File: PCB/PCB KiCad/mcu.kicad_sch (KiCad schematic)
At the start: 12 parts, among them J1 ADC Debug, J2 LED Debug, J3 Qwiic, SW1 MCU_RESET, SW2 TRIGGER

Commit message: PCB at time of order
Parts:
- R17: value 82 -> 150
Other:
- note added: "potential problem logic is at 5v potential solution logic level shifter"
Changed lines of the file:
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@@
     (effects (font (size 3 3)) (justify left bottom))
+  )
+  (text "potential problem\nlogic is at 5v\npotential solution\nlogic level shifter\n\n"
+    (at 129.54 100.33 0)
+    (effects (font (size 1.27 1.27)) (justify left bottom))
   )
   (text "Connectors" (at 39.37 148.59 0)
@@
       (effects (font (size 1.27 1.27)) (justify right))
     )
-    (property "Value" "82" (id 1) (at 213.36 48.8949 0)
-      (effects (font (size 1.27 1.27)) (justify right))
-    )
+    (property "Value" "150" (id 1) (at 213.36 48.8949 0)
+      (effects (font (size 1.27 1.27)) (justify right))
+    )

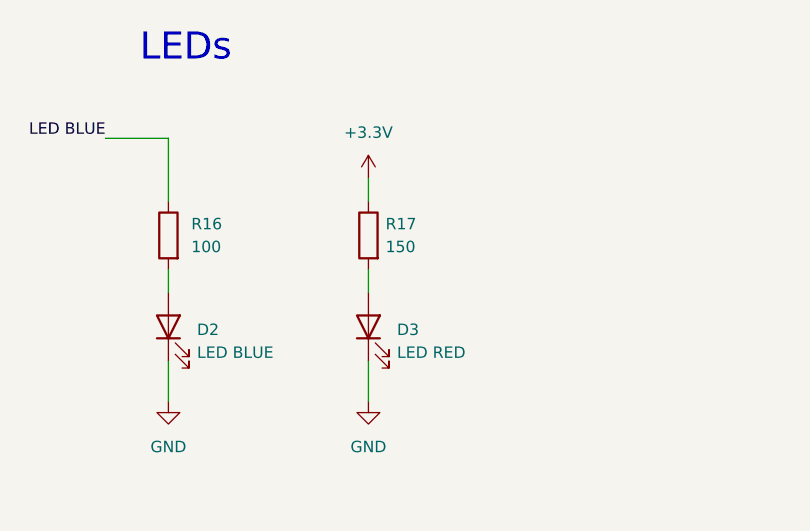
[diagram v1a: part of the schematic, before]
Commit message: Adds 1720nm datasheet and corrects some typ's
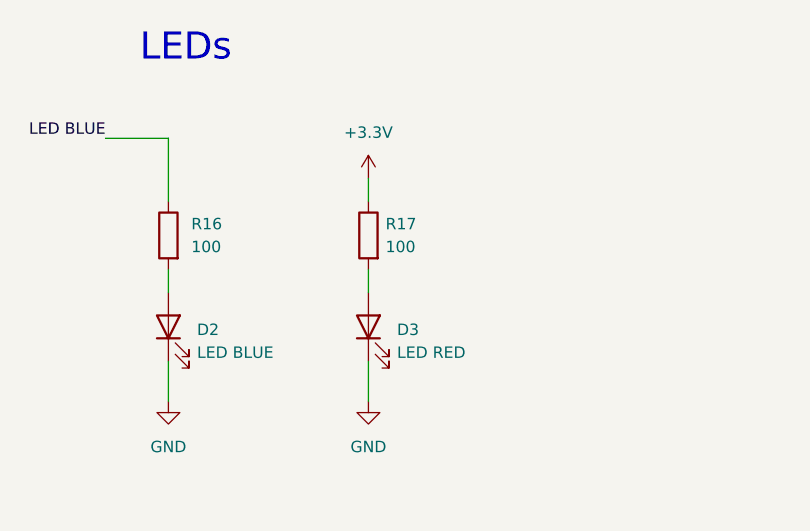
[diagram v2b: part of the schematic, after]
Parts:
- R17: value 150 -> 100
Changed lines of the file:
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@@
       (effects (font (size 1.27 1.27)) (justify right))
     )
-    (property "Value" "150" (id 1) (at 213.36 48.8949 0)
+    (property "Value" "100" (id 1) (at 213.36 48.8949 0)
       (effects (font (size 1.27 1.27)) (justify right))
     )

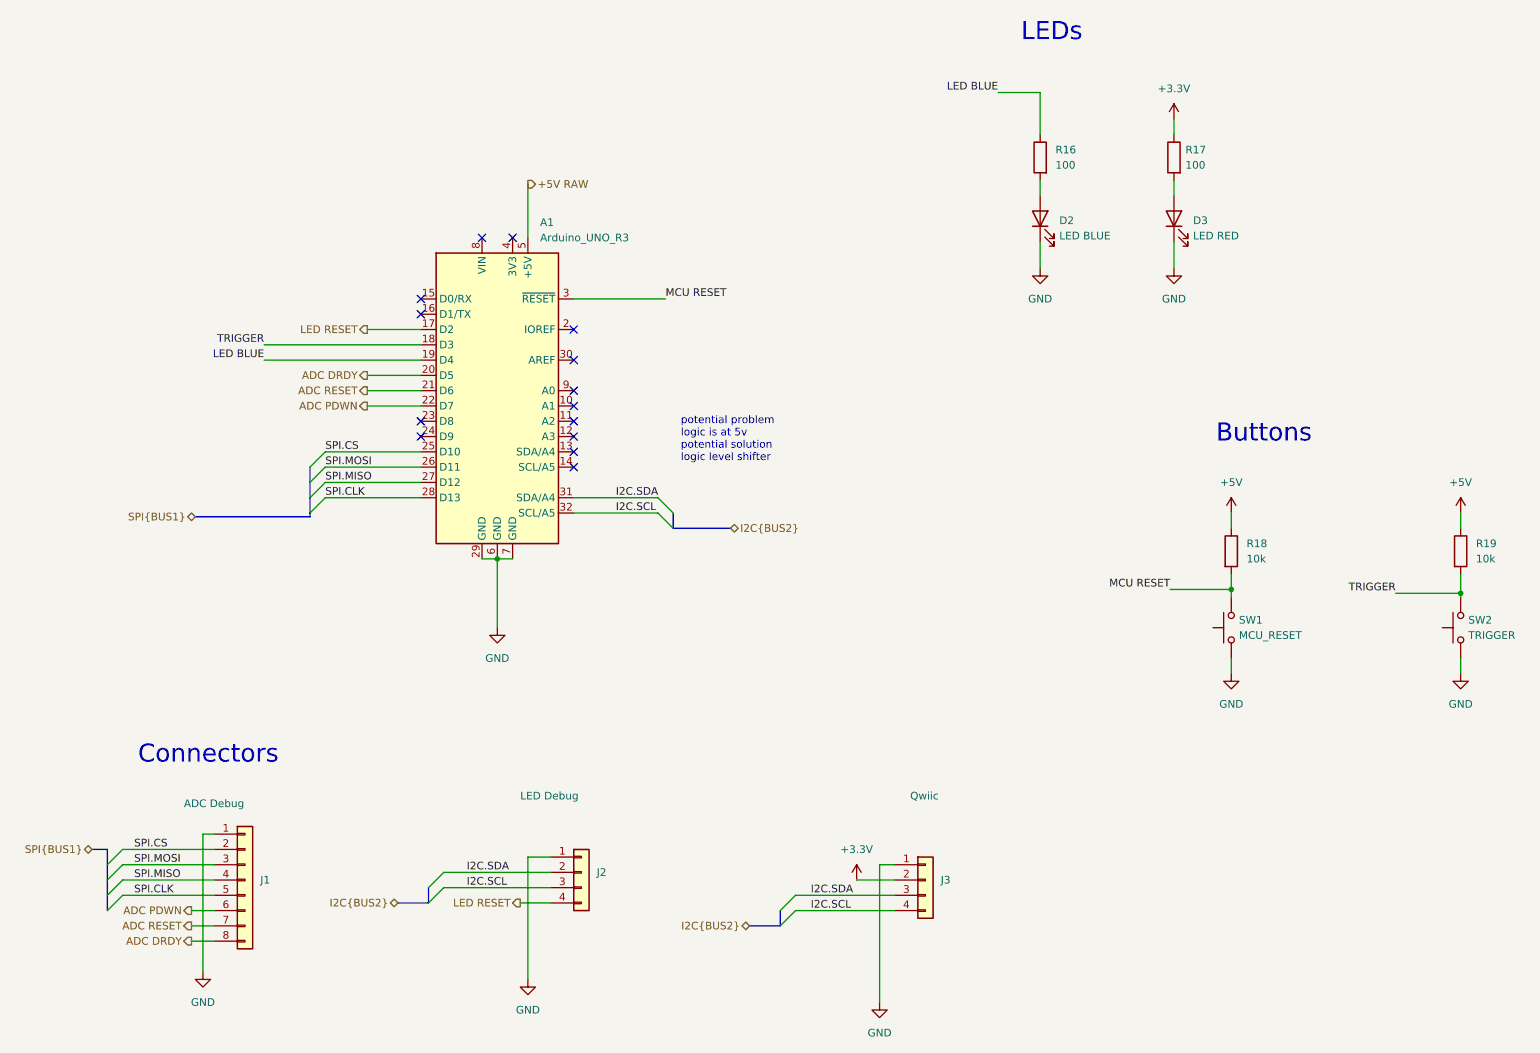
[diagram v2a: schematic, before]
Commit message: v2.2.0 first attempt for new ICs
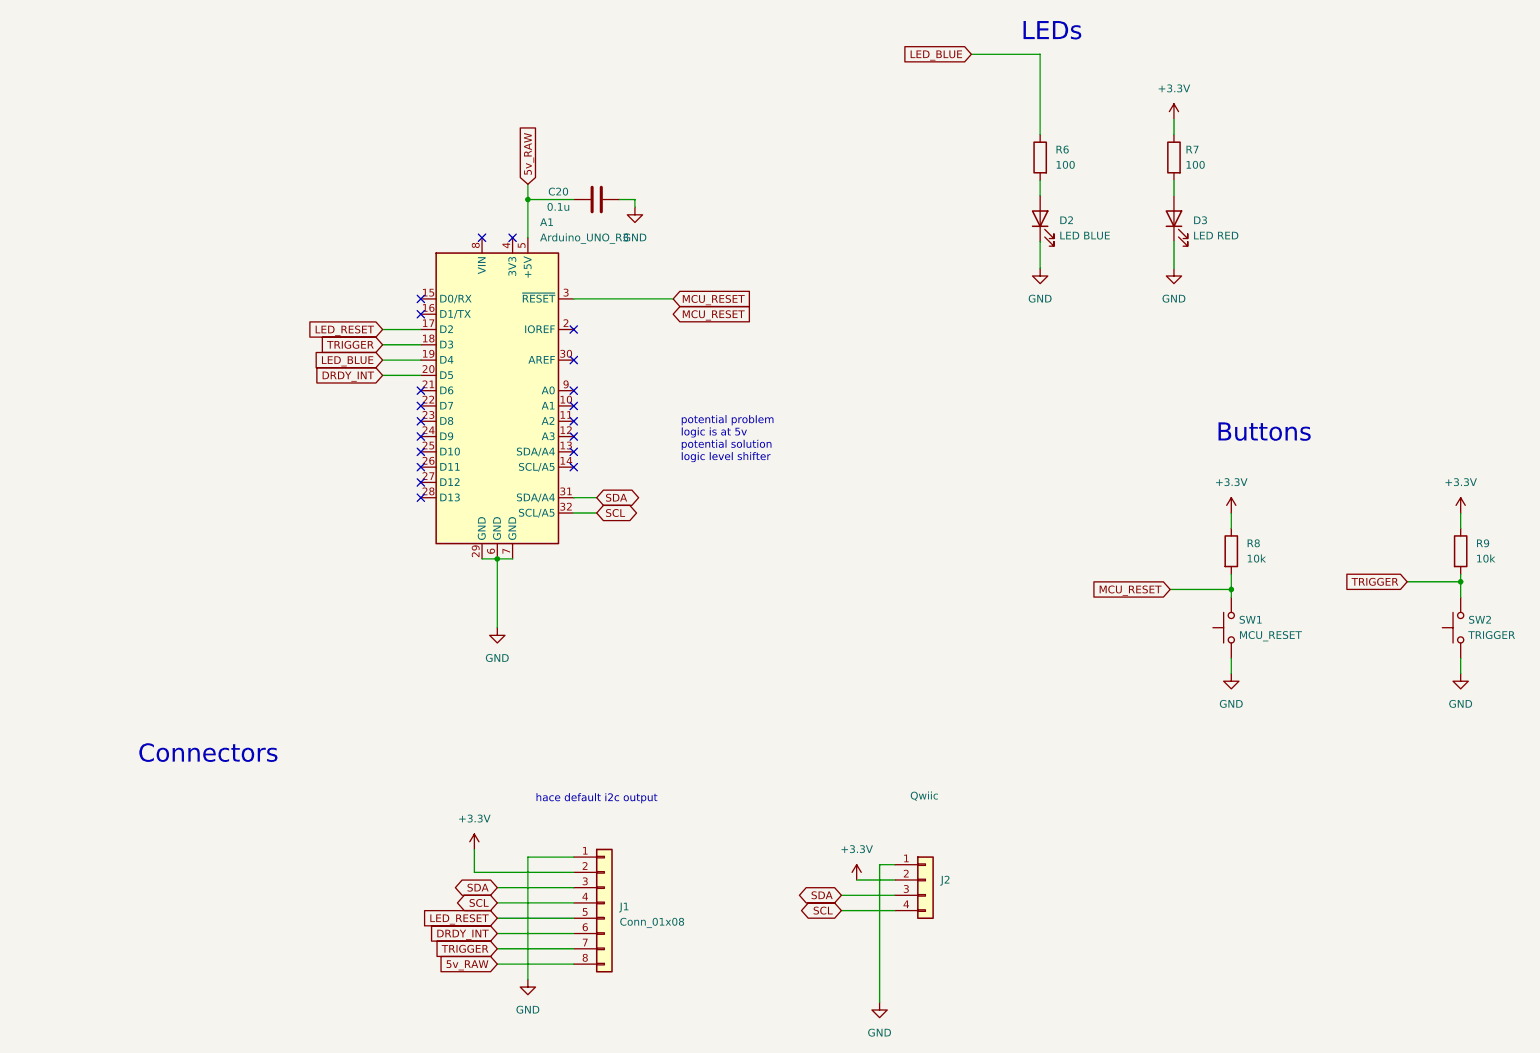
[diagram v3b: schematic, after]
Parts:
- removed J2: LED Debug, Connector_PinHeader_2.54mm:PinHeader_1x04_P2.54mm_Vertical, symbol Connector_Generic:Conn_01x04
- added C20: 0.1u, Capacitor_SMD:C_0805_2012Metric_Pad1.18x1.45mm_HandSolder, symbol Device:C
- J1: value ADC Debug -> Conn_01x08
- renumbered J3 to J2, R16 to R6, R17 to R7, R18 to R8, R19 to R9
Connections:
- net +5V is gone; now on net +3V3: R8.1, R9.1
- net +3V3: now also J1.2 (Pin_2)
- net GND: now also C20.2
- net TRIGGER: now also J1.7 (Pin_7)
- net +5V RAW renamed 5v_RAW
- net 5v_RAW: now also J1.8 (Pin_8), C20.1
- net ADC DRDY renamed DRDY_INT
- net DRDY_INT: now also J1.6 (Pin_6); no longer J1.8 (Pin_8)
- net ADC PDWN: no longer names the net of A1.22 (D7)
- net ADC PDWN: no longer J1.6 (Pin_6)
- net ADC RESET: no longer names the net of A1.21 (D6)
- net ADC RESET: no longer J1.7 (Pin_7)
- net I2C.SCL renamed SCL
- net SCL: now also J1.4 (Pin_4)
- net I2C.SDA renamed SDA
- net SDA: now also J1.3 (Pin_3)
- net LED BLUE renamed LED_BLUE
- net LED RESET renamed LED_RESET
- net LED_RESET: now also J1.5 (Pin_5)
- net MCU RESET renamed MCU_RESET
- net SPI.CLK: no longer names the net of A1.28 (D13)
- net SPI.CLK: no longer J1.5 (Pin_5)
- net SPI.CS: no longer names the net of A1.25 (D10)
- net SPI.CS: no longer J1.2 (Pin_2)
- net SPI.MISO: no longer names the net of A1.27 (D12)
- net SPI.MISO: no longer J1.4 (Pin_4)
- net SPI.MOSI: no longer names the net of A1.26 (D11)
- net SPI.MOSI: no longer J1.3 (Pin_3)
- no-connect marks 14 -> 20
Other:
- note added: "hace default i2c output"
